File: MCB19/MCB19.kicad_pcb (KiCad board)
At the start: 2 copper layers, 78 parts, among them J401 USART, J402 DISABLE, J601 RJ45, J602 RJ45, J611 +BATT, J612 GND, J613 VBAT+, J614 VBAT-, Q601 IRFP260N, Q602 IRFP260N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

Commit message: Novos detalhes na placa
Comecei a planejar onde ficam os componentes da placa, em especial os que fazem parte do buck e os que estão no atmega328p, exceto os do driver
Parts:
- moved R407 288.0 mm to (221.8, 57.8), turned to 270 degrees
- moved R408 285.4 mm to (219.2, 57.8), turned to 90 degrees
- moved C408 284.7 mm to (216.8, 57.7), turned to 90 degrees
- moved R409 281.1 mm to (226.8, 57.8), turned to 270 degrees
- moved R410 260.5 mm to (248.0, 77.0), turned to 90 degrees
- moved J402 248.1 mm to (244.0, 77.0), turned to 180 degrees
- moved J611 116.3 mm to (372.8, 264.8)
- moved D403 105.9 mm to (270.5, 84.0)
- moved D501 105.9 mm to (272.7, 52.6)
- moved J601 105.9 mm to (292.8, 58.7)
- moved R203 105.9 mm to (265.1, 61.3)
- moved TP205 105.9 mm to (265.1, 57.3)
- moved TP208 105.9 mm to (271.8, 60.6)
- moved U201 105.9 mm to (271.8, 69.5)
- moved U202 105.9 mm to (259.8, 69.5)
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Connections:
- R408 pad 1: /MCU/LM324_A -> Net-(C408-Pad1)
- R408 pad 2: Net-(C408-Pad1) -> /MCU/LM324_A
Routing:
- net Net-(C603-Pad1): track 0.00 -> 47.4 mm
- net GND: track 161.7 -> 141.9 mm
- net Net-(J402-Pad2): track 0.00 -> 19.1 mm
- net Net-(C407-Pad2): track 0.00 -> 11.3 mm
- net Net-(C408-Pad1): track 0.63 -> 9.50 mm
- net Net-(C601-Pad2): track 8.55 -> 0.10 mm
- added copper zone on B.Cu, net +BATT
- added copper zone on B.Cu, net Net-(C601-Pad2)

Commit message: Mudanças no layout
Arrumado um problema de portas trocadas
Layout modificado no driver
Proxima parte: Adicionar filtros para as medidas
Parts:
- moved R606 400.7 mm to (42.0, 91.0), turned to 270 degrees
- moved U602 370.5 mm to (47.0, 92.5), turned to 180 degrees
- moved U603 359.1 mm to (50.8, 76.8)
- moved J613 320.9 mm to (39.5, 124.5)
- moved J614 320.9 mm to (105.8, 162.9)
- moved Q602 318.4 mm to (155.7, 66.7), turned to 270 degrees
- moved L601 310.4 mm to (157.1, 72.2), turned to 90 degrees
- moved R601 309.3 mm to (172.0, 32.5), turned to 180 degrees
- moved R604 304.8 mm to (171.0, 58.2)
- moved U601 301.2 mm to (177.0, 35.0), turned to 90 degrees
- moved D603 293.5 mm to (172.8, 49.8), turned to 180 degrees
- moved Q601 293.4 mm to (164.2, 83.1), turned to 90 degrees
- moved C602 291.2 mm to (156.8, 83.8), turned to 180 degrees
- moved D601 278.7 mm to (181.2, 40.2), turned to 90 degrees
- moved DZ603 277.6 mm to (172.8, 52.8), turned to 180 degrees
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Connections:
- R408 pad 2: /MCU/LM324_A -> /driver/LM324A
- U401 pad 12: /driver/LM324A -> /MCU/PWM
- U601 pad 6: /driver/PWM -> /MCU/PWM
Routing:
- net GND: track 141.9 -> 229.5 mm
- net Net-(C601-Pad2): track 0.10 -> 37.0 mm, vias 0 -> 2
- net +5V: track 165.6 -> 199.0 mm
- net Net-(D602-Pad1): track 0.00 -> 22.8 mm
- net Net-(D603-Pad2): track 0.00 -> 17.0 mm, vias 0 -> 2
- net Net-(D603-Pad1): track 0.00 -> 16.8 mm
- net Net-(D602-Pad2): track 0.00 -> 16.6 mm
- net Net-(J613-Pad1): track 0.00 -> 10.8 mm
- net Net-(C601-Pad1): track 0.00 -> 8.46 mm
- net +BATT: track 17.3 -> 10.2 mm
- net Net-(C603-Pad1): track 47.4 -> 41.4 mm
- net Net-(DZ603-Pad1): track 0.00 -> 3.00 mm
- net Net-(DZ601-Pad1): track 0.00 -> 3.00 mm
- net Net-(R601-Pad1): track 0.00 -> 2.08 mm
- net Net-(U603-Pad5): track 0.00 -> 1.27 mm
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- added copper zone on B.Cu, net Net-(D602-Pad2)
- added copper zone on B.Cu, net Net-(D603-Pad2)
- removed copper zone on B.Cu, net +BATT
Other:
- net class Default: clearance 0.508 -> 0.4
- rule trace_clearance: 0.508 -> 0.4

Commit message: Add files via upload
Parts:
- added C604: 1uF, Capacitor_Tantalum_SMD:CP_EIA-6032-20_AVX-F_Pad2.25x2.35mm_HandSolder, B.Cu at (373.8, 125.2)
- added C605: 100nF, Capacitor_SMD:C_0805_2012Metric_Pad1.15x1.40mm_HandSolder, B.Cu at (375.3, 122.2)
- moved R605 233.2 mm to (376.6, 136.4)
- moved D603 226.0 mm to (380.2, 139.4), turned to 270 degrees
- moved DZ604 225.9 mm to (378.4, 149.2), turned to 90 degrees
- moved R603 225.2 mm to (376.6, 138.8)
- moved DZ603 224.6 mm to (375.6, 149.2), turned to 90 degrees
- moved R601 224.5 mm to (372.3, 133.9), turned to 0 degrees
- moved C601 218.6 mm to (376.6, 133.9), turned to 0 degrees
- moved R604 218.5 mm to (372.4, 143.0), turned to 180 degrees
- moved U601 218.5 mm to (373.8, 129.9), turned to 180 degrees
- moved D601 215.4 mm to (379.3, 124.9)
- moved Q602 212.4 mm to (350.4, 151.4), turned to 180 degrees
- moved DZ602 210.5 mm to (372.8, 149.2), turned to 90 degrees
- moved R602 209.8 mm to (372.3, 136.4), turned to 180 degrees
- moved DZ601 209.4 mm to (370.1, 149.2), turned to 90 degrees
- moved D602 205.0 mm to (368.8, 138.9), turned to 270 degrees
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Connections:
- DZ602 pad 2: Net-(C601-Pad2) -> GND
- DZ604 pad 2: GND -> Net-(C601-Pad2)
- Q601 pad 1: Net-(D602-Pad2) -> Net-(D603-Pad2)
- Q602 pad 1: Net-(D603-Pad2) -> Net-(D602-Pad2)
- R604 pad 1: Net-(C601-Pad2) -> GND
- R605 pad 1: GND -> Net-(C601-Pad2)
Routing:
- net GND: track 229.5 -> 306.3 mm
- net Net-(C601-Pad2): track 37.0 -> 105.9 mm, vias 2 -> 0
- net +BATT: track 10.2 -> 37.0 mm
- net Net-(C603-Pad1): track 41.4 -> 18.6 mm
- net Net-(D602-Pad2): track 16.6 -> 37.3 mm
- net +5V: track 199.0 -> 212.0 mm, vias 6 -> 8
- net Net-(D602-Pad1): track 22.8 -> 12.3 mm
- net Net-(D603-Pad1): track 16.8 -> 14.3 mm, vias 0 -> 2
- net Net-(D603-Pad2): track 17.0 -> 14.7 mm, vias 2 -> 0
- net Net-(C601-Pad1): track 8.46 -> 9.93 mm
- removed copper zone on B.Cu, net Net-(C601-Pad2)
- removed copper zone on B.Cu, net Net-(D602-Pad2)
- removed copper zone on B.Cu, net Net-(D603-Pad2)

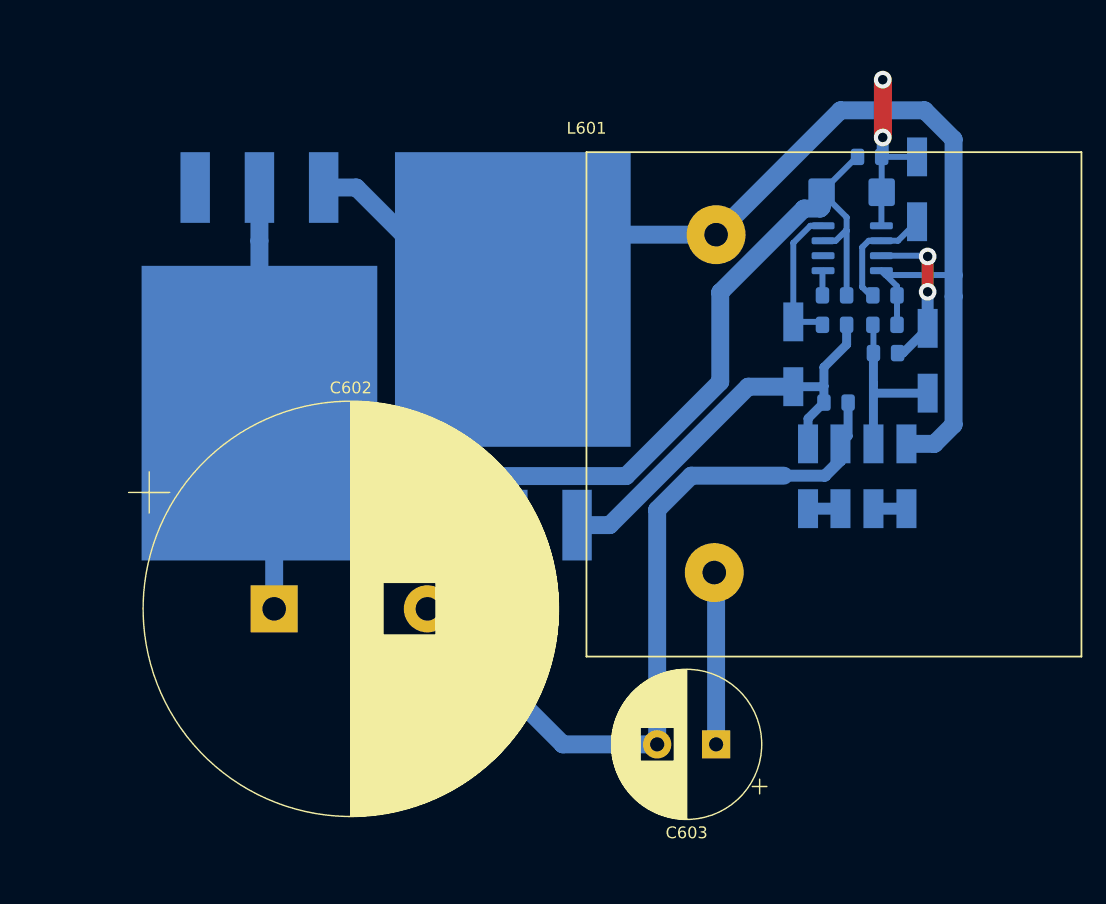
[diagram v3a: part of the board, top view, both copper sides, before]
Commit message: Novo design
Foi realizada uma nova topologia para a placa, diminuindo trilhas de alta importância
Ainda faltam algumas partes do circuito
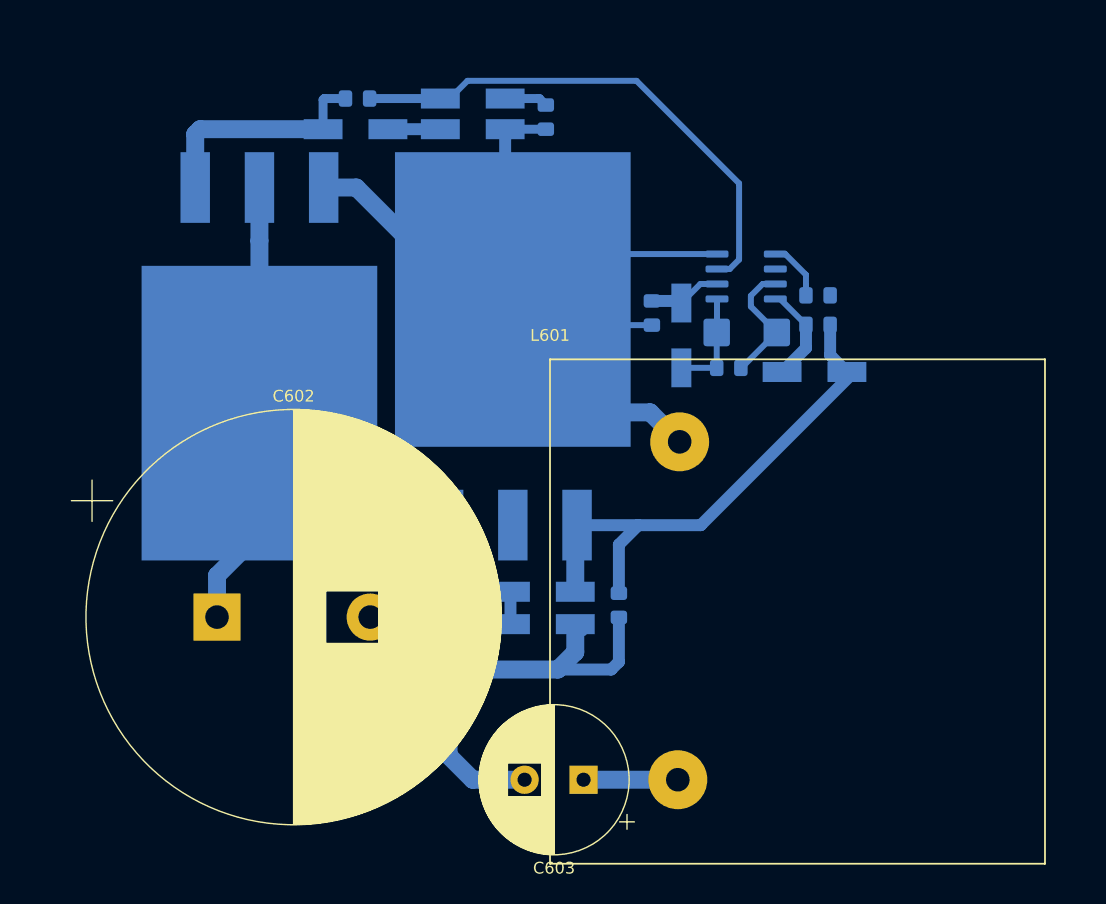
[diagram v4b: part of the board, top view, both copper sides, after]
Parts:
- moved DZ603 52.9 mm to (331.6, 119.8), turned to 180 degrees
- moved R603 49.7 mm to (331.8, 117.2)
- moved DZ604 47.1 mm to (341.6, 119.8), turned to 0 degrees
- moved D603 44.6 mm to (341.6, 117.2), turned to 0 degrees
- moved R605 33.7 mm to (347.8, 118.8), turned to 90 degrees
- moved DZ602 28.2 mm to (347.6, 161.8), turned to 0 degrees
- moved R604 25.2 mm to (354.0, 160.2), turned to 90 degrees
- moved DZ601 24.5 mm to (347.6, 159.1), turned to 0 degrees
- moved D601 23.5 mm to (359.3, 137.3), turned to 270 degrees
- moved C605 21.5 mm to (363.3, 140.1), turned to 0 degrees
- moved C601 19.8 mm to (356.8, 135.4), turned to 270 degrees
- moved L601 17.8 mm to (348.2, 139.3)
- moved C604 14.9 mm to (364.9, 137.1), turned to 0 degrees
- moved C603 11.6 mm to (351.0, 175.0)
- moved U601 9.31 mm to (364.8, 132.3), turned to 0 degrees
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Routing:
- net GND: track 306.3 -> 234.9 mm
- net Net-(D603-Pad1): track 14.3 -> 44.2 mm, vias 2 -> 0
- net Net-(C601-Pad2): track 105.9 -> 88.9 mm
- net Net-(D602-Pad2): track 37.3 -> 46.5 mm
- net Net-(D603-Pad2): track 14.7 -> 23.7 mm
- net Net-(C603-Pad1): track 18.6 -> 11.9 mm
- net +5V: track 212.0 -> 205.5 mm, vias 8 -> 6
- net Net-(D602-Pad1): track 12.3 -> 8.35 mm
- net Net-(C601-Pad1): track 9.93 -> 6.27 mm
- net Net-(R601-Pad1): track 2.12 -> 5.08 mm
- net Net-(DZ603-Pad1): track 2.80 -> 4.45 mm
- net +BATT: track 37.0 -> 37.9 mm

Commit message: Final
Design de layout pronto
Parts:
- added C606: 47nF, Capacitor_SMD:C_0805_2012Metric_Pad1.15x1.40mm_HandSolder, B.Cu at (107.4, 95.6)
- added C607: 47nF, Capacitor_SMD:C_0805_2012Metric_Pad1.15x1.40mm_HandSolder, B.Cu at (107.4, 105.4)
- added D604: LL4148, Diode_SMD:D_MiniMELF_Handsoldering, B.Cu at (104.8, 93.0)
- added D605: LL4148, Diode_SMD:D_MiniMELF_Handsoldering, B.Cu at (104.8, 102.8)
- added R607: 1R, Resistor_SMD:R_0805_2012Metric_Pad1.15x1.40mm_HandSolder, B.Cu at (107.4, 91.2)
- added R608: 1R, Resistor_SMD:R_0805_2012Metric_Pad1.15x1.40mm_HandSolder, B.Cu at (107.4, 101.0)
- added R609: 470R, Resistor_SMD:R_0805_2012Metric_Pad1.15x1.40mm_HandSolder, B.Cu at (88.2, 93.0)
- added R610: 1k5, Resistor_SMD:R_0805_2012Metric_Pad1.15x1.40mm_HandSolder, B.Cu at (88.2, 90.6)
- moved C603 287.0 mm to (80.8, 78.2), turned to 90 degrees
- moved R604 270.2 mm to (95.6, 81.2), turned to 0 degrees
- moved DZ602 268.1 mm to (94.0, 74.8), turned to 270 degrees
- moved DZ601 264.6 mm to (96.8, 74.8), turned to 270 degrees
- moved D602 258.7 mm to (115.4, 97.8), turned to 270 degrees
- moved Q602 256.9 mm to (104.4, 77.7), turned to 90 degrees
- moved R602 254.4 mm to (119.4, 98.1), turned to 90 degrees
- moved C602 253.2 mm to (94.6, 48.6), turned to 270 degrees
- moved C605 252.5 mm to (115.8, 90.5), turned to 270 degrees
- moved R601 251.6 mm to (121.9, 98.1), turned to 270 degrees
- moved C604 250.2 mm to (118.8, 92.0), turned to 270 degrees
- moved D601 246.1 mm to (118.5, 86.5), turned to 180 degrees
- moved U601 244.6 mm to (123.5, 92.0), turned to 270 degrees
- moved C601 241.9 mm to (120.4, 84.0), turned to 180 degrees
- moved L601 240.4 mm to (116.5, 75.4), turned to 270 degrees
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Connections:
- U401 pad 12: /MCU/PWM -> Net-(U401-Pad12)
- U401 pad 28: Net-(U401-Pad28) -> /MCU/PWM
- U603 pad 3: Net-(J613-Pad1) -> Net-(R609-Pad2)
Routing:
- net /driver/LM324A: track 0.00 -> 81.0 mm, vias 0 -> 2
- net /MCU/INALLL: track 0.00 -> 71.7 mm, vias 0 -> 2
- net GND: track 234.9 -> 295.7 mm, vias 10 -> 14
- net /POWER SUPPLY/+18V_IN: track 62.4 -> 3.51 mm
- net Net-(J613-Pad1): track 10.8 -> 67.9 mm
- net /CANBUS CONN/CAN_18V: track 0.00 -> 54.3 mm
- net +BATT: track 37.9 -> 83.0 mm
- net +5V: track 205.5 -> 249.9 mm, vias 6 -> 8
- net /MCU/PWM: track 0.00 -> 27.7 mm, vias 0 -> 2
- net /SCK: track 36.8 -> 63.8 mm
- net /CANBUS/INT: track 22.4 -> 44.2 mm
- net Net-(D602-Pad2): track 46.5 -> 64.9 mm
- net /MOSI: track 34.2 -> 52.5 mm
- net Net-(C601-Pad2): track 88.9 -> 106.8 mm
- net /MISO: track 39.0 -> 54.7 mm
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- added copper zone on B.Cu, net +BATT
- added copper zone on B.Cu, net GND

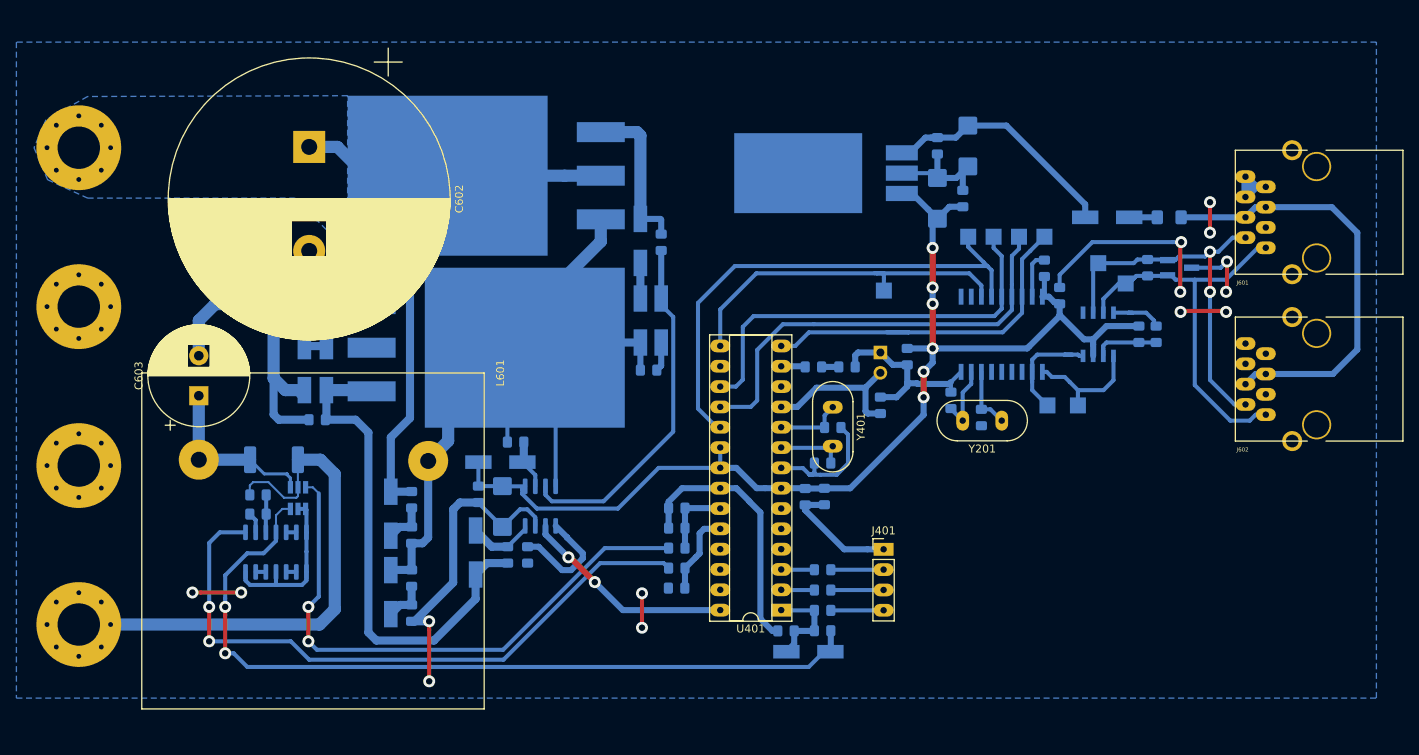
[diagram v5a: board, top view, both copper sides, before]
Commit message: Final refeito Remodelagem de trilhas e acertos de distancias Sera necessario uma verificação das malhas
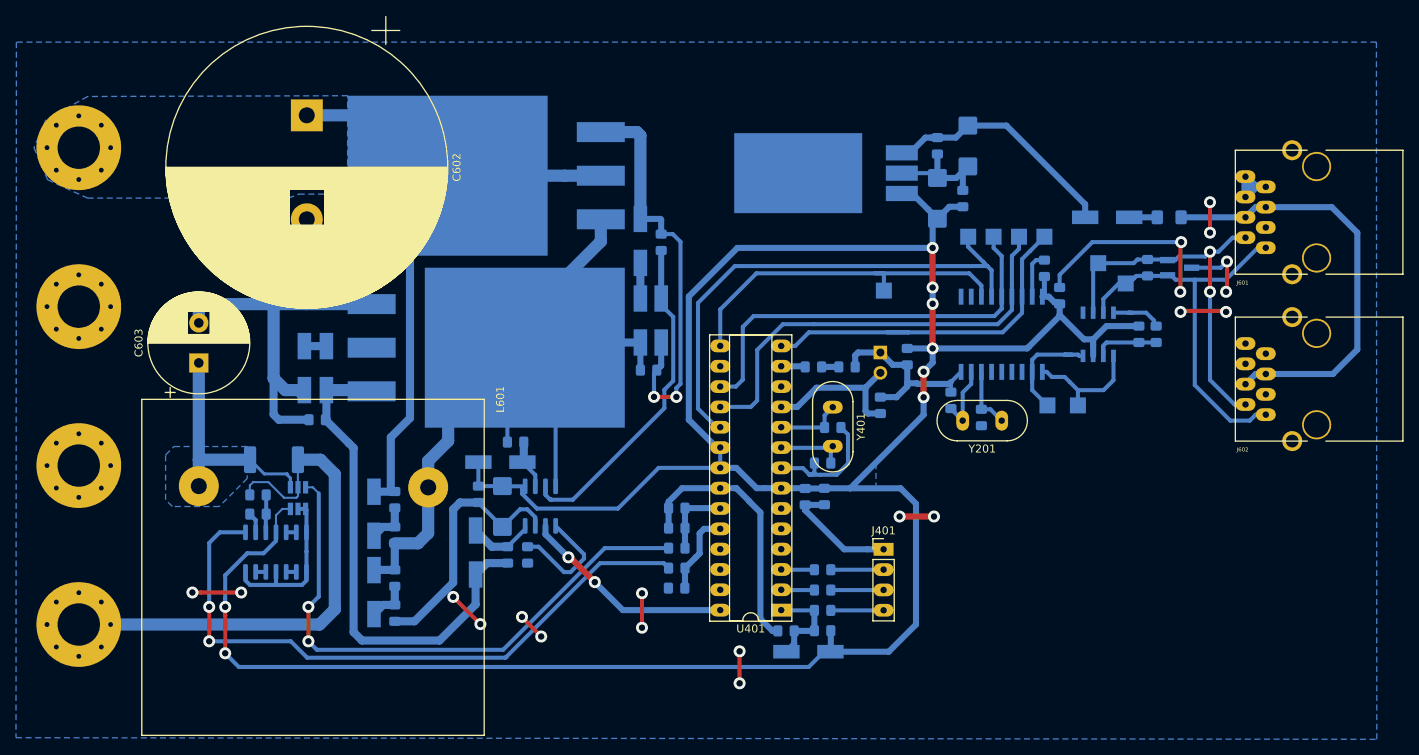
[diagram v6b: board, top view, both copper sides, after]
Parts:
- moved C603 4.10 mm to (80.8, 74.1)
- moved C602 3.96 mm to (94.3, 44.6)
- moved L601 3.30 mm to (116.5, 78.7)
- moved C606 2.10 mm to (105.3, 95.6)
- moved C607 2.10 mm to (105.3, 105.4)
- moved R607 2.10 mm to (105.3, 91.2)
- moved R608 2.10 mm to (105.3, 101.0)
- moved D604 2.10 mm to (102.7, 93.0)
- moved D605 2.10 mm to (102.7, 102.8)
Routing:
- net +5V: track 249.9 -> 339.9 mm
- net Net-(D603-Pad2): track 23.7 -> 52.4 mm, vias 0 -> 2
- net GND: track 295.7 -> 305.1 mm, vias 14 -> 20
- net Net-(C603-Pad1): track 21.6 -> 29.0 mm
- net Net-(D603-Pad1): track 44.2 -> 41.7 mm
- net +BATT: track 83.0 -> 84.9 mm
- net Net-(C601-Pad2): track 106.8 -> 108.6 mm
- net Net-(D602-Pad2): track 64.9 -> 64.2 mm
- added copper zone on B.Cu, net +5V
- added copper zone on B.Cu, net Net-(C603-Pad1)

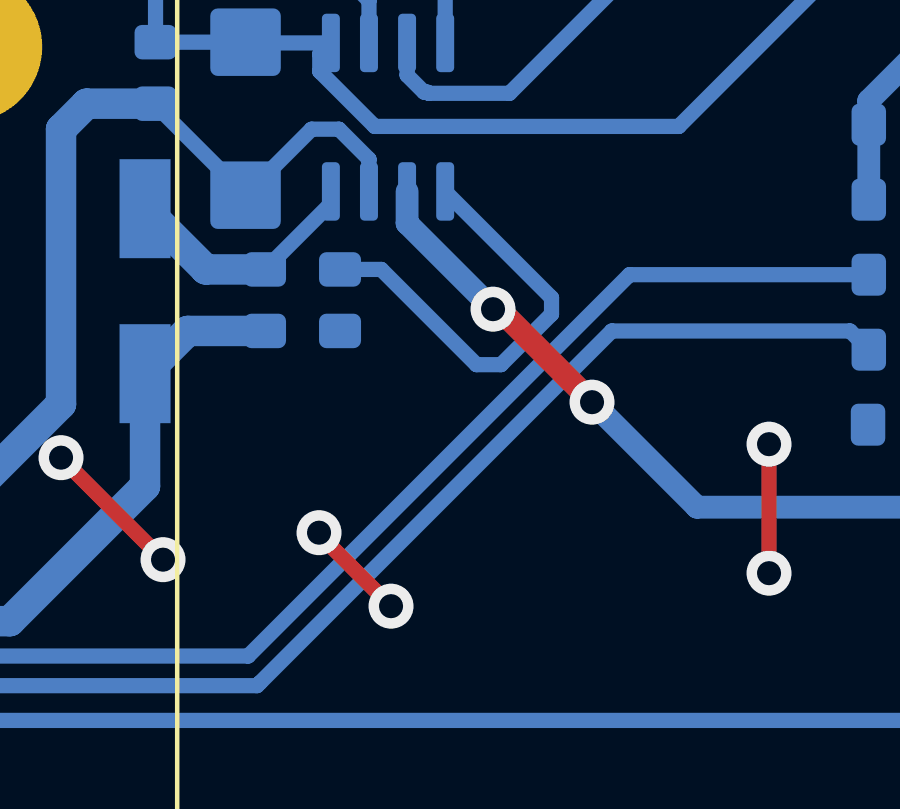
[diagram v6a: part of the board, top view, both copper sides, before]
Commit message: Verificação de trilhas na regiao do indutor OK
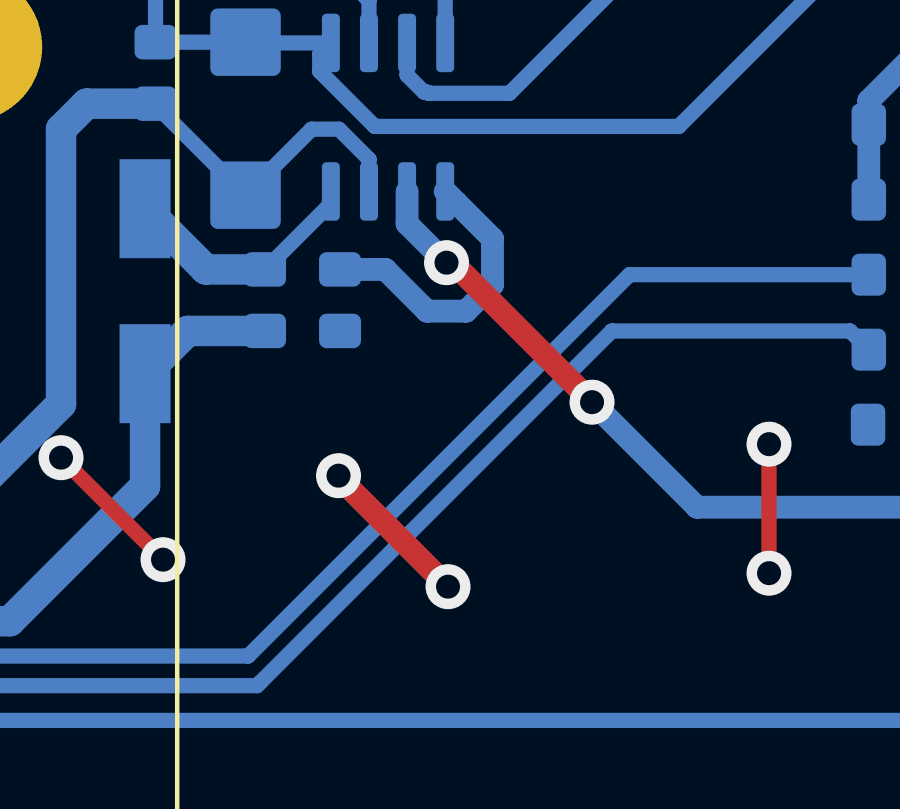
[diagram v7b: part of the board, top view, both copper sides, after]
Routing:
- net Net-(R601-Pad1): track 14.6 -> 9.78 mm
- net GND: track 305.1 -> 306.8 mm

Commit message: Terminando os detalhes ajustes de malha e trilha tem que ser verificado
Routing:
- net GND: track 306.8 -> 306.1 mm
